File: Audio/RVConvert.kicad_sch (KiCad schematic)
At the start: 2 parts, among them J29 Conn_01x06_Pin, J30 Conn_01x06_Pin

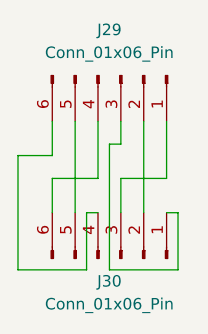
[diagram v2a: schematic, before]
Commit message: ヘッドホン出力と切替を追加し、S式検査をコミット前に走らせる。
Amp 後段を PHONE/MUTE/LINE に分け、NJM4556A の電流バッファとパッド付きボリュームを載せる。括弧崩れで回路図が開けなくなるのを check_sexpr と pre-commit で止める。

Co-authored-by: Cursor <cursoragent@cursor.com>
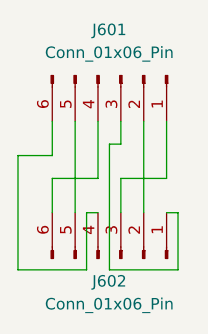
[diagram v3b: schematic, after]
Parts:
- renumbered J29 to J601, J30 to J602
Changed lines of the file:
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@@
 		(dnp no)
 		(fields_autoplaced yes)
-		(property "Reference" "J29"
+		(property "Reference" "J601"
 			(at 53.34 48.26 90)
 			(show_name no)
@@
 			(project "AudioCase"
 				(path "/760b9589-09e7-434e-9ca2-6e4136e3b7a2/e27346ec-040d-41ba-b795-0891abf25329"
-					(reference "J29")
+					(reference "J601")
 					(unit 1)
 				)
@@
 		(in_pos_files yes)
 		(dnp no)
-		(property "Reference" "J30"
+		(property "Reference" "J602"
 			(at 53.34 76.2 90)
 			(show_name no)
@@
 			(project "AudioCase"
 				(path "/760b9589-09e7-434e-9ca2-6e4136e3b7a2/e27346ec-040d-41ba-b795-0891abf25329"
-					(reference "J30")
+					(reference "J602")
 					(unit 1)
 				)
